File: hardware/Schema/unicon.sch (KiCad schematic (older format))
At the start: 94 parts, among them J1 PROG, J2 PWR, J3 SIDE A, J4 SIDE B, U1 LM340MP-5.0, U2 SIP21106-3.3, U3 STM32F051C8Tx, U4 AT24C16, U5 ST485B, U6 ULN2003A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

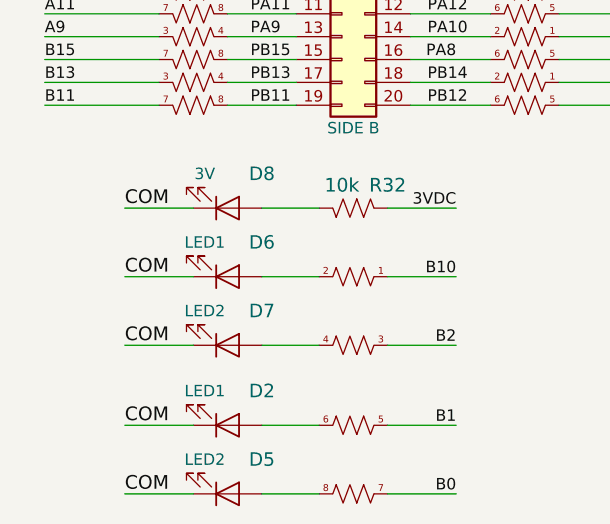
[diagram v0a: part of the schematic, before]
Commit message: pervadinti sviesos diodai
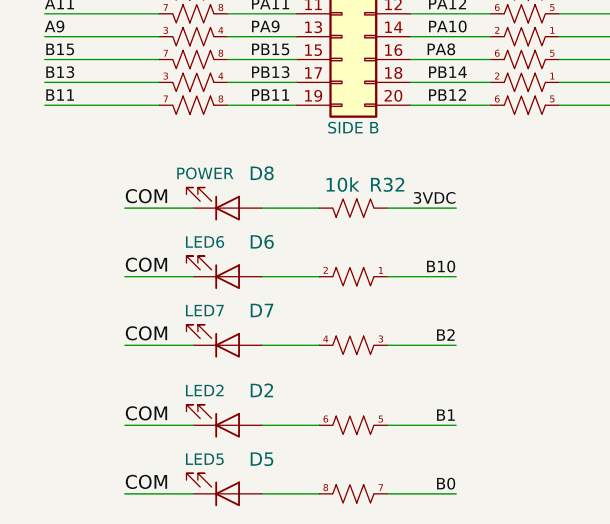
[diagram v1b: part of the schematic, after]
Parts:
- D2: value LED1 -> LED2
- D5: value LED2 -> LED5
- D6: value LED1 -> LED6
- D7: value LED2 -> LED7
- D8: value 3V -> POWER
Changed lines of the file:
@@
 LIBS:various
 LIBS:resistors
+LIBS:LED
 LIBS:power
 LIBS:device
@@
 LIBS:contrib
 LIBS:valves
+LIBS:Diode
+LIBS:Display
 LIBS:unicon-cache
 EELAYER 25 0
@@
 P 1750 10050
 F 0 "D2" H 1900 9900 59  0000 C CNN
-F 1 "LED1" H 1650 9900 50  0000 C CNN
+F 1 "LED2" H 1650 9900 50  0000 C CNN
 F 2 "disc:LED_0805" H 2600 9900 50  0001 C CNN
 F 3 "" H 1750 10150 50  0001 C CNN
@@
 P 1750 10350
 F 0 "D5" H 1900 10200 59  0000 C CNN
-F 1 "LED2" H 1650 10200 50  0000 C CNN
+F 1 "LED5" H 1650 10200 50  0000 C CNN
 F 2 "disc:LED_0805" H 2600 10200 50  0001 C CNN
 F 3 "" H 1750 10450 50  0001 C CNN
@@
 P 1750 9400
 F 0 "D6" H 1900 9250 59  0000 C CNN
-F 1 "LED1" H 1650 9250 50  0000 C CNN
+F 1 "LED6" H 1650 9250 50  0000 C CNN
 F 2 "disc:LED_0805" H 2600 9250 50  0001 C CNN
 F 3 "" H 1750 9500 50  0001 C CNN
@@
 P 1750 9700
 F 0 "D7" H 1900 9550 59  0000 C CNN
-F 1 "LED2" H 1650 9550 50  0000 C CNN
+F 1 "LED7" H 1650 9550 50  0000 C CNN
 F 2 "disc:LED_0805" H 2600 9550 50  0001 C CNN
 F 3 "" H 1750 9800 50  0001 C CNN
@@
 P 1750 9100
 F 0 "D8" H 1900 8950 59  0000 C CNN
-F 1 "3V" H 1650 8950 50  0000 C CNN
+F 1 "POWER" H 1650 8950 50  0000 C CNN
 F 2 "disc:LED_0805" H 2600 8950 50  0001 C CNN
 F 3 "" H 1750 9200 50  0001 C CNN
